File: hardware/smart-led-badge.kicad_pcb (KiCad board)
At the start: 4 copper layers, 112 x 74 mm, 1269 parts, among them J301 TYPE-C-31-M-12, J302 Battery JST-PH 2P, J501 SWD 2x5 1.27mm, Q201 AO3401A, Q202 AO3400A, Q203 AO3401A, Q204 AO3400A, Q301 AO3400A, Q302 AO3400A, Q303 AO3400A, Q701 AO3401A, Q702 AO3401A, Q703 AO3401A, Q704 AO3401A, Q705 AO3401A, Q706 AO3401A, Q707 AO3401A, Q708 AO3401A, Q709 AO3401A, Q710 AO3401A, Q711 AO3401A, Q712 AO3401A, Q713 AO3401A, Q714 AO3401A, Q715 AO3401A, Q716 AO3401A, Q717 AO3401A, Q718 AO3401A, Q719 AO3401A, Q720 AO3401A, Q721 AO3401A, Q722 AO3401A, Q723 AO3401A, Q724 AO3401A, Q725 AO3401A, Q726 AO3401A, Q727 AO3401A, Q728 AO3401A, Q729 AO3401A, Q730 AO3401A, Q731 AO3401A, Q732 AO3401A, SW1201 Mode/Next, SW1202 Action/Select, SW201 PCM12SMTR, U1101 NT3H2111W0FHKH, U201 TPS63802, U202 TPS61023, U301 TPD4E05U06, U302 BQ25620, U401 E73-2G4M08S1C, U601 TLC59283, U602 TLC59283, U701 SN74LVC8T245, U702 SN74HC595, U703 SN74HC595, U704 SN74HC595, U705 SN74HC595, U706 SN74LVC1G123, U707 SN74LVC1G04, U708 SN74LVC1G32, U901 ICM-42688-P, Y401 32.768kHz 9pF

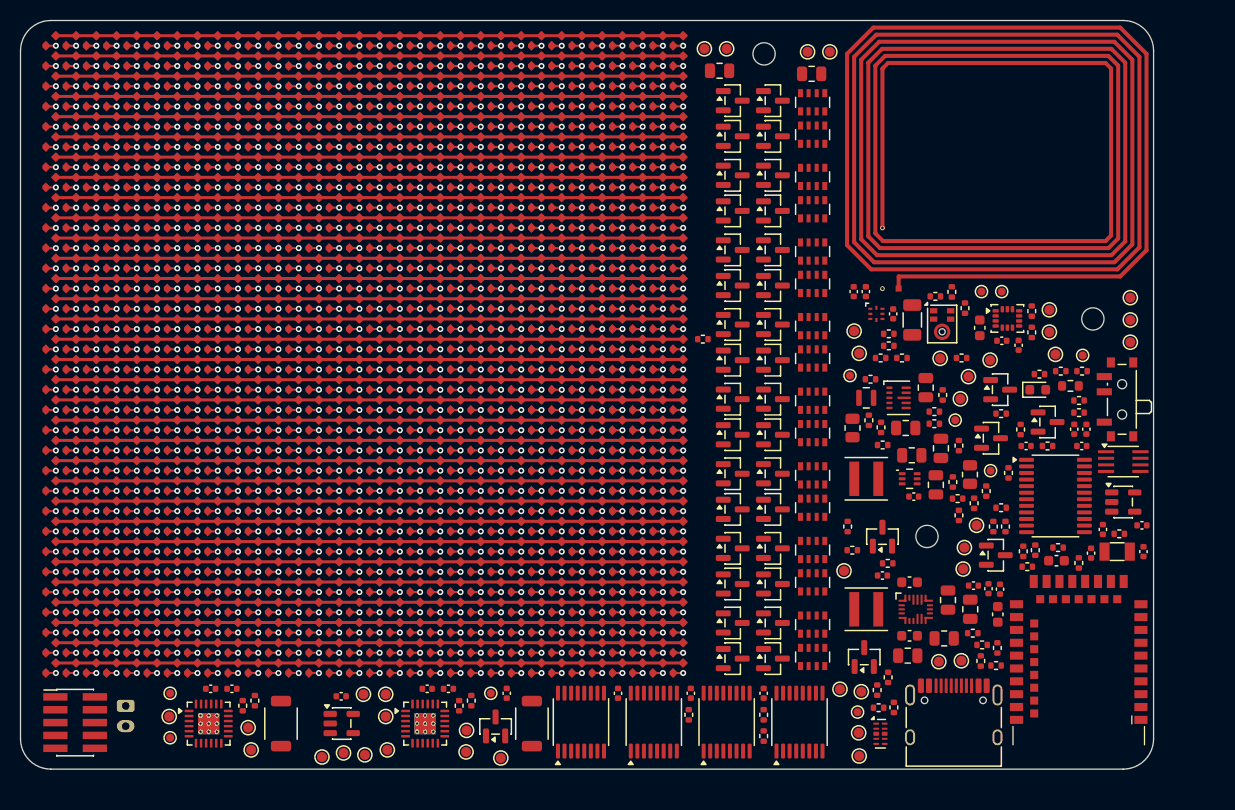
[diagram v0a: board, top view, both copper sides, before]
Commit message: hw: lay out and route the Rev A board (#29)
* hw: add fab-layer references to custom footprints

Show each part's reference on F.Fab so the assembly drawing used for
bring-up and rework labels the custom parts the same way as the KiCad
library parts. Copper, courtyards and silkscreen are unchanged.

* hw: join the NFC coil's twin pad-2 ends as a jumper

The coil's inner and outer pad-2 ends are connected by footprint copper
(the In1 crossover), which KiCad does not count as a connection, so
NFC_LB stayed unrouted. Treat the duplicate pad numbers as a jumper.
The pad 1/2 net tie is unchanged.

* hw: remove unfitted parts and spare test points

Free routing room on the Rev A board:
- remove the eight DNP row pull-down arrays (RN709-RN716) and six DNP
  passive positions (C1103, R1005, R1104, R212, R213, R310)
- remove 19 test points outside the required set that had no room on
  the routed board

No net changes and no fitted-part changes, so the assembled board and
its BOM are the same. C1102 stays as the DNP NFC tuning position.

* hw: lay out and route the Rev A board

Place and route the 118 x 76 mm four-layer board: the 32 x 32 matrix at
45 degrees on the west, the row drivers in a column beside it, and the
power, charger, NFC, IMU, microphone and E73 module on the east. In1 is
a GND plane kept solid under the regulators, charger and module; a few
low-current signals cross it elsewhere where no other layer had room.
The board uses the JLC04161H-7628 stack-up, tented vias and
0.45/0.2 mm minimum vias.

Add release silkscreen: battery polarity at J302 on both faces,
test-point net names (front where they fit, rear behind each pad),
orientation-independent control marks, the board name and a designer
monogram on the NFC coil.

DRC and schematic parity are clean. Nothing is measured yet: charger,
USB, matrix timing, RF and NFC tuning remain bring-up checks. The README
and hardware docs now give the 118 x 76 mm outline.

* hw: move three vias out of component pads

The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
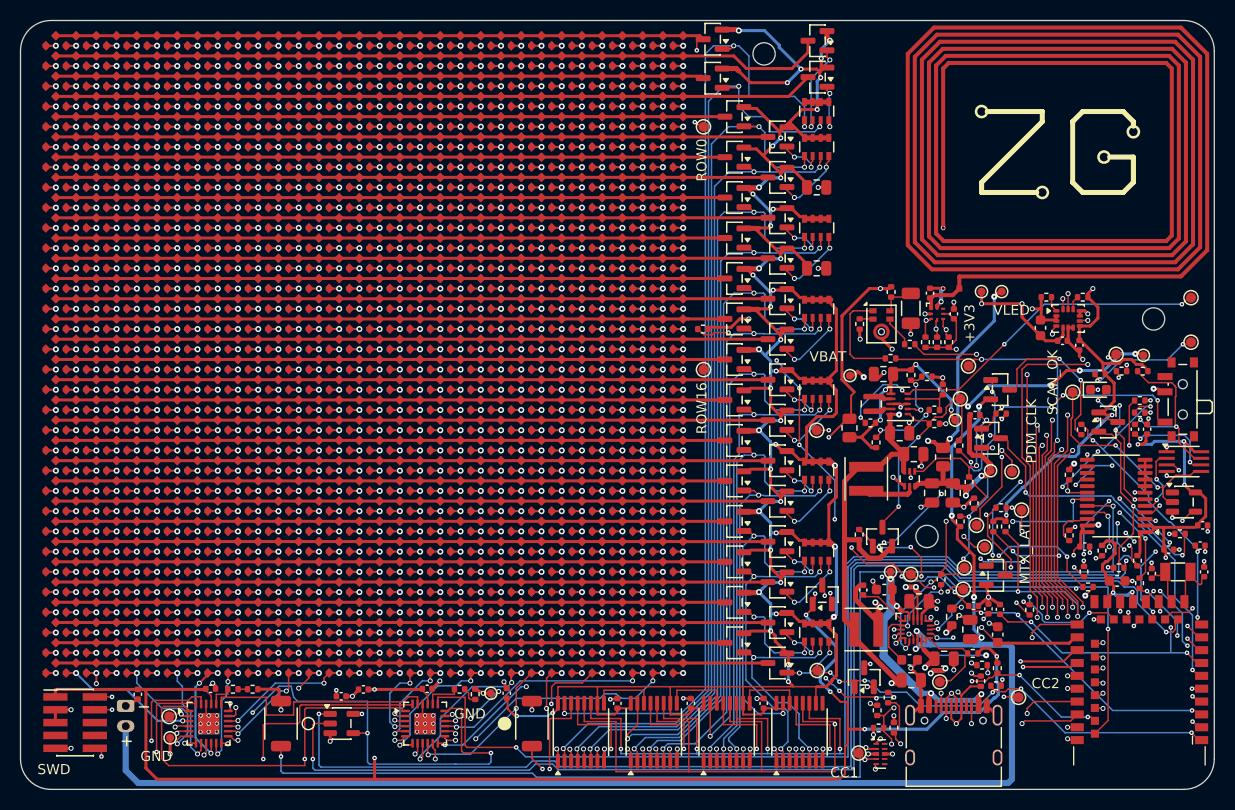
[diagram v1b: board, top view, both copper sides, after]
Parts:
- removed C1103: DNP, Capacitor_SMD:C_0402_1005Metric
- removed R1005, R1104, R212, R213, R310: DNP, Resistor_SMD:R_0402_1005Metric
- removed RN709, RN710, RN711, RN712, RN713, RN714, RN715, RN716: DNP, Resistor_SMD:R_Array_Convex_4x0603
- removed TP1101: NFC_PWR, TestPoint:TestPoint_Pad_D1.0mm
- removed TP1102: NFC_SDA, TestPoint:TestPoint_Pad_D1.0mm
- removed TP1103: NFC_SCL, TestPoint:TestPoint_Pad_D1.0mm
- removed TP1104: NFC_FD, TestPoint:TestPoint_Pad_D1.0mm
- removed TP211: LED_EN, TestPoint:TestPoint_Pad_D1.0mm
- removed TP215: SW_ON, TestPoint:TestPoint_Pad_D1.0mm
- removed TP302: PMID, smart-led-badge:TestPoint_Pad_D0.8mm
- removed TP306: CHG_PG_N, TestPoint:TestPoint_Pad_D1.0mm
- removed TP312: I2C1_SDA, TestPoint:TestPoint_Pad_D1.0mm
- removed TP313: I2C1_SCL, TestPoint:TestPoint_Pad_D1.0mm
- removed TP602: COL31, TestPoint:TestPoint_Pad_D1.0mm
- removed TP603: IREF1, TestPoint:TestPoint_Pad_D1.0mm
- removed TP604: IREF2, TestPoint:TestPoint_Pad_D1.0mm
- removed TP606: MTX_MOSI, TestPoint:TestPoint_Pad_D1.0mm
- removed TP702: BLANK_TLC, TestPoint:TestPoint_Pad_D1.0mm
- removed TP705: SER_V, TestPoint:TestPoint_Pad_D1.0mm
- removed TP706: SRCLK_V, TestPoint:TestPoint_Pad_D1.0mm
- removed TP707: RCLK_V, TestPoint:TestPoint_Pad_D1.0mm
- removed TP710: ROW31, TestPoint:TestPoint_Pad_D1.0mm
- moved TP301 72.2 mm to (136.0, 104.5)
- moved TP307 55.4 mm to (138.0, 104.8)
- moved R1201 43.9 mm to (156.9, 102.4)
- moved TP704 42.6 mm to (154.0, 86.8)
- moved R1202 40.8 mm to (160.4, 103.4)
- moved R705 38.4 mm to (153.7, 94.9)
- moved TP216 37.4 mm to (128.7, 90.5)
- moved Q302 34.8 mm to (129.2, 106.8)
- moved TP310 33.4 mm to (148.7, 116.9)
- moved TP214 32.4 mm to (128.8, 114.2)
- moved TP709 31.7 mm to (117.5, 84.5)
- moved R401 25.7 mm to (142.1, 109.0), turned to 90 degrees
- moved TP605 20.0 mm to (145.3, 102.0)
- moved C708 19.2 mm to (128.7, 74.5)
- moved TP1001 19.0 mm to (148.0, 94.6)
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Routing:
- net VLED: track 0.00 -> 336.9 mm, vias 0 -> 49
- net +3V3: track 0.00 -> 317.0 mm, vias 0 -> 22
- net MTX_SCK: track 0.00 -> 163.4 mm, vias 0 -> 5
- net MTX_LAT: track 0.00 -> 160.4 mm, vias 0 -> 7
- net VBAT: track 0.00 -> 159.6 mm, vias 0 -> 7
- net MTX_SAFE_SENSE: track 0.00 -> 150.5 mm, vias 0 -> 7
- net MTX_BLANK: track 0.00 -> 144.7 mm, vias 0 -> 7
- net MTX_MOSI: track 0.00 -> 139.6 mm, vias 0 -> 2
- net BTN_MODE: track 0.00 -> 124.0 mm, vias 0 -> 4
- net nRESET: track 0.00 -> 113.8 mm, vias 0 -> 2
- net SWDIO: track 0.00 -> 112.0 mm, vias 0 -> 2
- net GND: track 0.00 -> 109.7 mm, vias 0 -> 79
- net /Matrix Row Drivers and Safety/SRCLK_V: track 0.00 -> 109.7 mm, vias 0 -> 5
- net SWDCLK: track 0.00 -> 108.0 mm, vias 0 -> 2
- net MTX_MISO: track 0.00 -> 107.7 mm, vias 0 -> 4
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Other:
- board size 112 x 74 mm -> 118 x 76 mm
- board text added: "+3V3"
- board text added: "3V3_REG"
- board text added: "CC1"
- board text added: "CC2"
- board text added: "CHG_STAT"
- board text added: "COL0"
- board text added: "EN_3V3"
- board text added: "GND"
- board text added: "MTX_BLANK"
- board text added: "MTX_LAT"
- board text added: "MTX_SAFE_SENSE"
- board text added: "MTX_SCK"
- board text added: "PDM_CLK"
- board text added: "PDM_DIN"
- board text added: "PG_3V3"
- board text added: "PWR_SW_N"
- board text added: "QON"
- board text added: "ROW0"
- board text added: "ROW16"
- board text added: "SCAN_OK"
- board text added: "SMART LED BADGE REV A"
- board text added: "SWD"
- board text added: "SYS"
- board text added: "TS"
- board text added: "VBAT"
- board text added: "VBAT_MEAS_EN"
- board text added: "VBAT_SENSE"
- board text added: "VBUS"
- board text added: "VLED"
- board text added: "VLED_REG"
- board text added: "VLED_SENSE"
